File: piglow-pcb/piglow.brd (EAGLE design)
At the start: 36.8 x 33.7 mm, 30 parts, among them IC1 SN3218, P1 led-pink-0805, P2 led-pink-0805, P3 led-pink-0805, Y1 led-yellow-0805, Y2 led-yellow-0805, Y3 led-yellow-0805

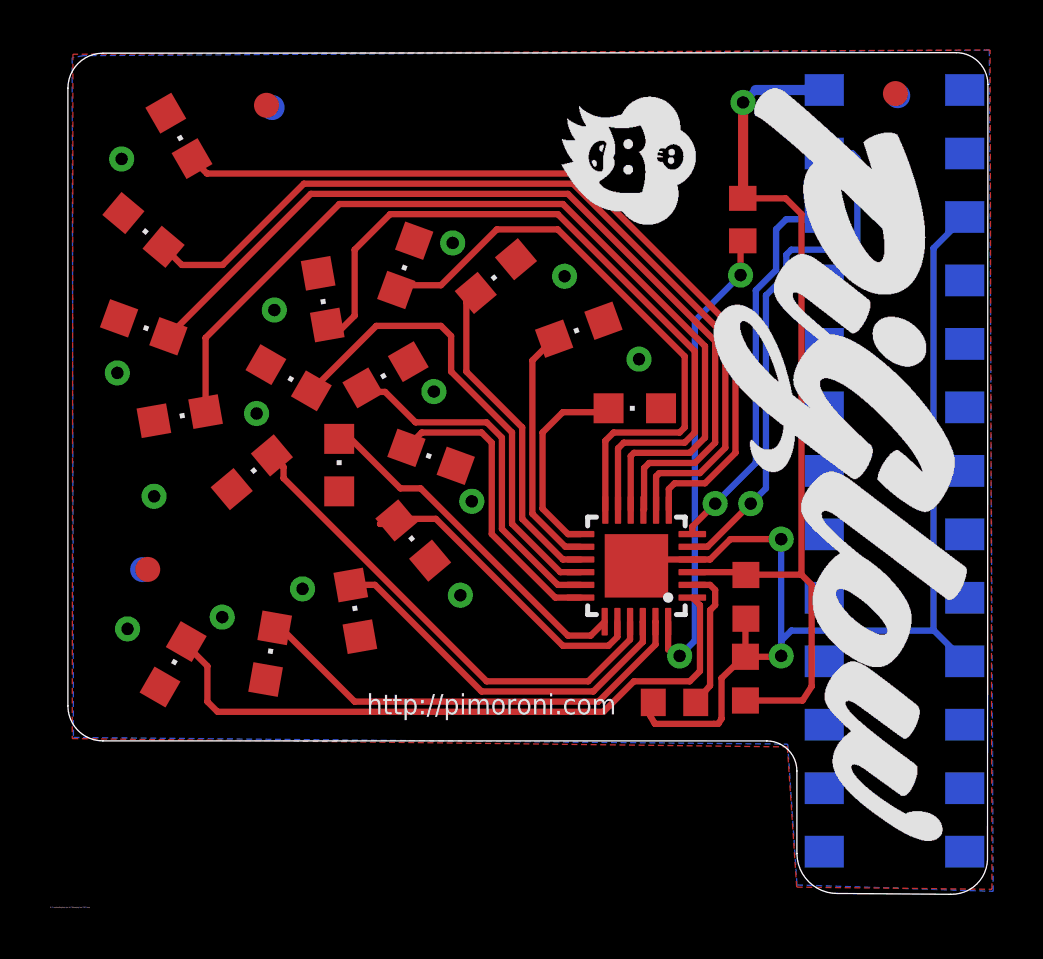
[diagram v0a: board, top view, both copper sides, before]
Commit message: Revert "Updated SN3218 to new landings"
This reverts commit 9275a731dc1cb28da2cd379615e04127a905d690.
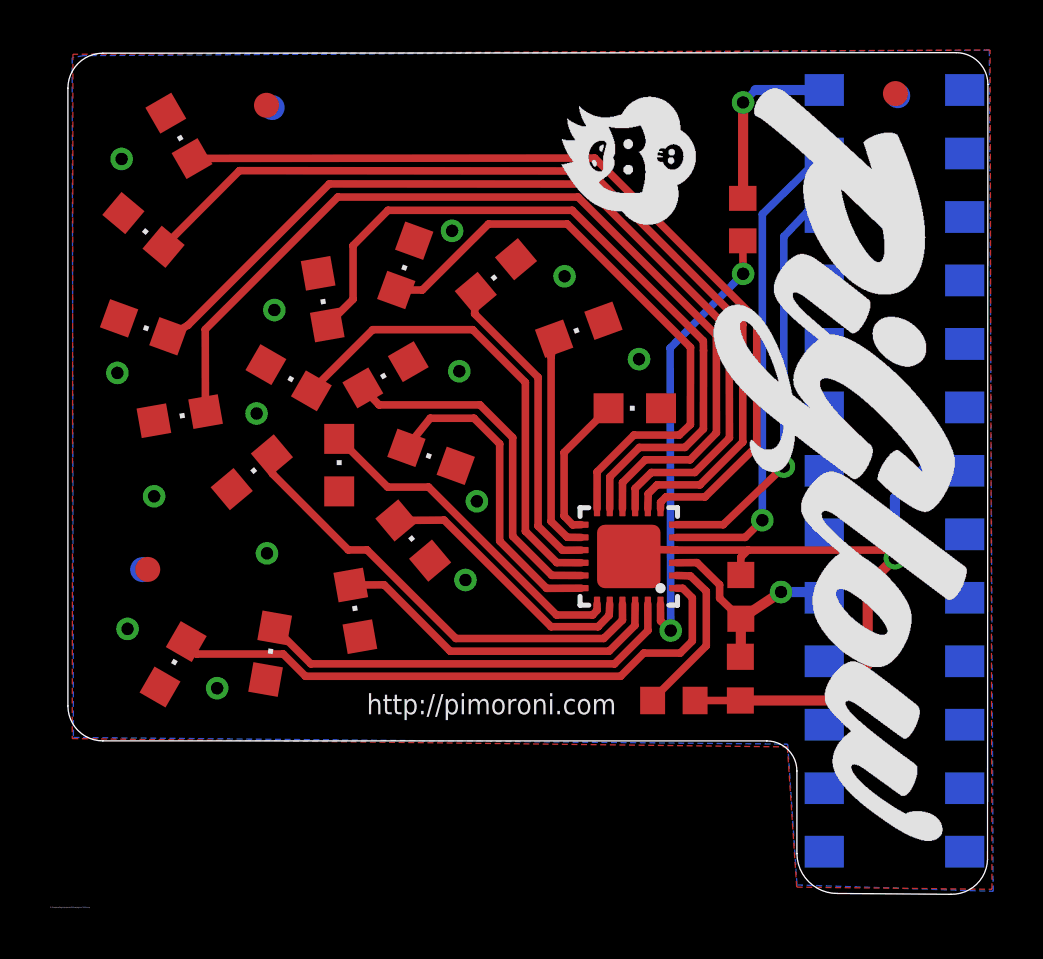
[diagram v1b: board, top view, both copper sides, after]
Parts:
- C1: value 100nf -> cercap-100nf-0603
- C2: value 1uF -> cercap-1uF-0603
- IC1: value SN3218 -> ic-sm3218-qfn24
- R4: value 3.3k -> res-3.3k-0603
- R5: value 10k -> res-10k-0603
- moved IC1 0.48 mm to (23.2, 13.9)
- moved C1 0.20 mm to (27.6, 9.05)
- moved C2 0.20 mm to (27.6, 12.3)
- moved R4 0.08 mm to (25.0, 8.17)
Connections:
- net SCL renamed N$1
- net SDA renamed N$2
- net SDB renamed N$3
- removed net 3V3: C1.1, C2.1, IC1.3, R5.2, U$4.P1_3V3
- removed net P17_3V3: U$4.P17_3V3
- removed net R_EXT: IC1.2, R4.2
- new net N$19: IC1.2, R4.1
- new net N$23: C1.2, C2.2, IC1.3, U$4.P17_3V3
- new net P4_5V: U$4.P4_5V
- new net VCC: R5.2, U$4.P1_3V3
- net 5V: no longer U$4.P4_5V
- net GND: now also C1.1, C2.1, R4.2; no longer C1.2, C2.2, R4.1, U$4.P20_GND, U$4.P6_GND
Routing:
- net 3V3: track 36.9 -> 0.00 mm, vias 1 -> 0
- net GND: track 48.0 -> 29.9 mm, vias 2 -> 1
- net N$23: track 0.00 -> 9.26 mm, vias 0 -> 1
- net VCC: track 0.00 -> 7.49 mm, vias 0 -> 1
- net N$19: track 0.00 -> 6.70 mm
- net R_EXT: track 5.80 -> 0.00 mm
- net N$4: track 26.4 -> 24.0 mm
- net N$22: track 13.2 -> 10.9 mm
- net N$14: track 8.04 -> 5.88 mm
- net N$8: track 33.6 -> 35.7 mm
- net N$2: track 21.5 -> 19.4 mm
- net N$10: track 35.7 -> 37.1 mm
- net N$6: track 15.1 -> 13.8 mm
- net N$7: track 19.7 -> 18.4 mm
- net N$3: track 19.3 -> 18.0 mm
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
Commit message: Updated SN3218 to new landings
Also Tidied up Schematic and rerouted board with 10mil traces and 8mil
clearance
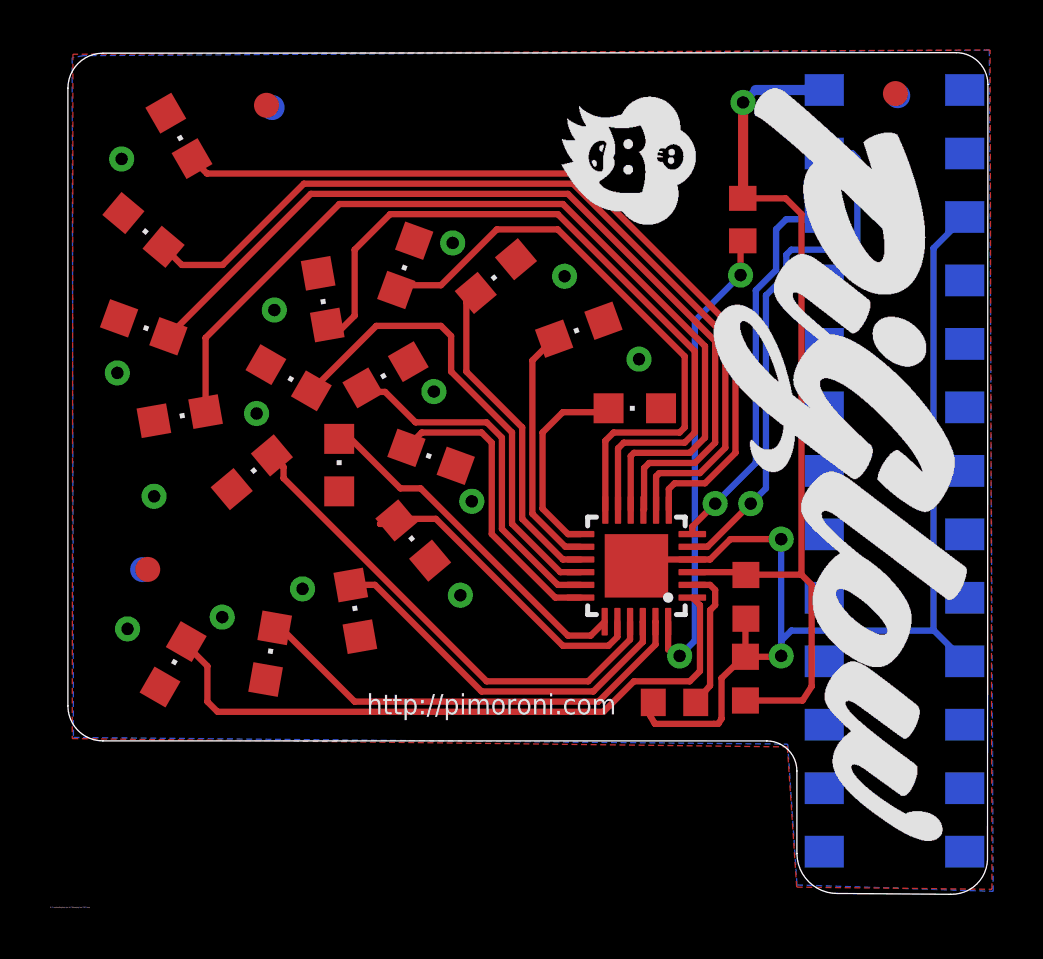
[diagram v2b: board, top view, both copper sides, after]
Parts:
- C1: value cercap-100nf-0603 -> 100nf
- C2: value cercap-1uF-0603 -> 1uF
- IC1: value ic-sm3218-qfn24 -> SN3218
- R4: value res-3.3k-0603 -> 3.3k
- R5: value res-10k-0603 -> 10k
- moved IC1 0.48 mm to (23.5, 13.6)
- moved C1 0.20 mm to (27.8, 9.05)
- moved C2 0.20 mm to (27.8, 12.3)
- moved R4 0.08 mm to (25.0, 8.10)
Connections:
- net N$1 renamed SCL
- net N$2 renamed SDA
- net N$3 renamed SDB
- removed net N$19: IC1.2, R4.1
- removed net N$23: C1.2, C2.2, IC1.3, U$4.P17_3V3
- removed net P4_5V: U$4.P4_5V
- removed net VCC: R5.2, U$4.P1_3V3
- new net 3V3: C1.1, C2.1, IC1.3, R5.2, U$4.P1_3V3
- new net P17_3V3: U$4.P17_3V3
- new net R_EXT: IC1.2, R4.2
- net 5V: now also U$4.P4_5V
- net GND: now also C1.2, C2.2, R4.1, U$4.P20_GND, U$4.P6_GND; no longer C1.1, C2.1, R4.2
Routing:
- net 3V3: track 0.00 -> 36.9 mm, vias 0 -> 1
- net GND: track 29.9 -> 48.0 mm, vias 1 -> 2
- net N$23: track 9.26 -> 0.00 mm, vias 1 -> 0
- net VCC: track 7.49 -> 0.00 mm, vias 1 -> 0
- net N$19: track 6.70 -> 0.00 mm
- net R_EXT: track 0.00 -> 5.80 mm
- net N$4: track 24.0 -> 26.4 mm
- net N$22: track 10.9 -> 13.2 mm
- net N$14: track 5.88 -> 8.04 mm
- net N$8: track 35.7 -> 33.6 mm
- net SDA: track 19.4 -> 21.5 mm
- net N$10: track 37.1 -> 35.7 mm
- net N$6: track 13.8 -> 15.1 mm
- net N$7: track 18.4 -> 19.7 mm
- net SDB: track 18.0 -> 19.3 mm
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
